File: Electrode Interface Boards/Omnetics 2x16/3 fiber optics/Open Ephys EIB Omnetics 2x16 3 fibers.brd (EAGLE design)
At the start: 16.1 x 16.1 mm, 40 parts

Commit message: Add Gerber files and images for EIBs
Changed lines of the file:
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@@
 <?xml version="1.0" encoding="utf-8"?>
 <!DOCTYPE eagle SYSTEM "eagle.dtd">
-<eagle version="6.1">
+<eagle version="6.3">
 <drawing>
 <settings>
@@
 <setting verticaltext="up"/>
 </settings>
-<grid distance="5" unitdist="mil" unit="mil" style="lines" multiple="1" display="yes" altdistance="0.005" altunitdist="inch" altunit="inch"/>
+<grid distance="1" unitdist="mil" unit="mil" style="lines" multiple="1" display="yes" altdistance="0.005" altunitdist="inch" altunit="inch"/>
 <layers>
-<layer number="1" name="Top" color="4" fill="1" visible="yes" active="yes"/>
+<layer number="1" name="Top" color="11" fill="1" visible="yes" active="yes"/>
 <layer number="16" name="Bottom" color="1" fill="1" visible="yes" active="yes"/>
 <layer number="17" name="Pads" color="2" fill="1" visible="yes" active="yes"/>
@@
 <layer number="23" name="tOrigins" color="15" fill="1" visible="yes" active="yes"/>
 <layer number="24" name="bOrigins" color="15" fill="1" visible="yes" active="yes"/>
-<layer number="25" name="tNames" color="7" fill="1" visible="yes" active="yes"/>
+<layer number="25" name="tNames" color="3" fill="1" visible="yes" active="yes"/>
 <layer number="26" name="bNames" color="7" fill="1" visible="yes" active="yes"/>
 <layer number="27" name="tValues" color="7" fill="1" visible="yes" active="yes"/>
@@
 <wire x1="19.685" y1="20.193" x2="21.082" y2="19.05" width="0.254" layer="25"/>
 <wire x1="21.082" y1="19.05" x2="21.844" y2="19.05" width="0.254" layer="25"/>
-<circle x="25.4" y="25.4" radius="8.0645" width="0.2032" layer="20"/>
+<circle x="25.4" y="25.4" radius="8.0645" width="0.0508" layer="20"/>
 <text x="20.701" y="26.416" size="1.143" layer="25" font="vector" ratio="15">fopt</text>
 <text x="21.082" y="23.368" size="1.143" layer="25" font="vector" ratio="15">eib</text>
@@
 </class>
 </classes>
-<designrules>
+<designrules name="default">
 <description language="de">&lt;b&gt;EAGLE Design Rules&lt;/b&gt;
 &lt;p&gt;

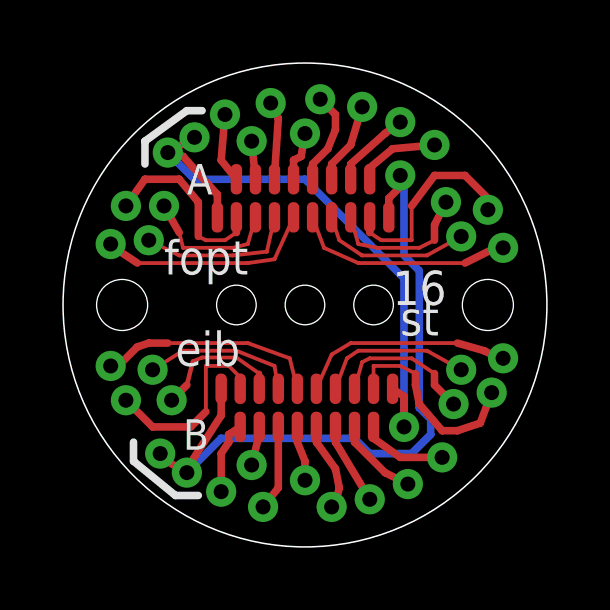
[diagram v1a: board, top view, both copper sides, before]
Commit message: Fix spacing issues on 2x16 boards
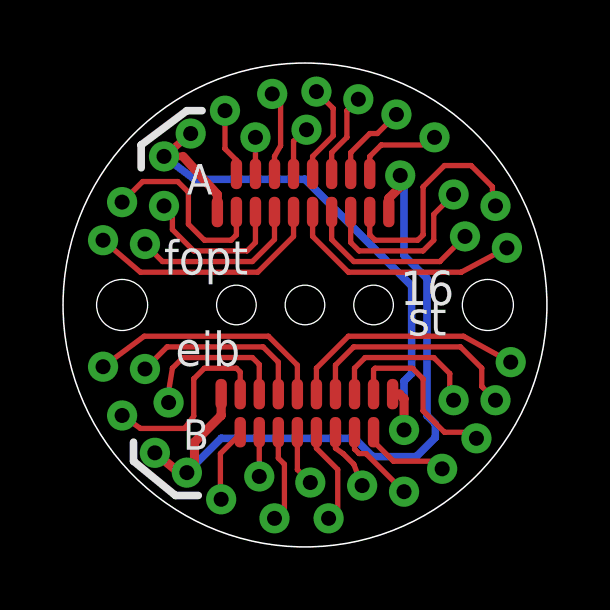
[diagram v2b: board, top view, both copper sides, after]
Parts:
- moved U$3 1.61 mm to (31.1, 21.0)
- moved U$4 1.53 mm to (31.8, 22.2)
- moved U$16 0.54 mm to (24.4, 18.3)
- moved U$10 0.52 mm to (19.3, 21.7)
- moved U$13 0.52 mm to (27.3, 19.4)
- moved U$17 0.46 mm to (23.9, 19.7)
- moved U$14 0.39 mm to (26.2, 18.3)
- moved U$11 0.38 mm to (30.0, 19.9)
- moved U$25 0.36 mm to (30.4, 29.1)
- moved U$34 0.31 mm to (24.3, 32.4)
- moved U$29 0.28 mm to (27.2, 32.3)
- moved U$6 0.28 mm to (32.3, 23.5)
- moved U$26 0.28 mm to (31.8, 28.7)
- moved U$12 0.28 mm to (28.7, 19.2)
- moved U$28 0.28 mm to (28.4, 31.8)
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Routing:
- net N$5: track 5.14 -> 7.65 mm
- net N$7: track 7.14 -> 8.18 mm
- net N$19: track 6.87 -> 7.87 mm
- net N$3: track 6.81 -> 5.86 mm
- net N$20: track 4.90 -> 5.85 mm
- net N$8: track 5.12 -> 6.03 mm
- net N$9: track 4.45 -> 5.31 mm
- net N$6: track 7.17 -> 8.00 mm
- net N$21: track 5.19 -> 6.01 mm
- net N$23: track 7.29 -> 8.05 mm
- net N$16: track 2.73 -> 2.11 mm
- net N$22: track 7.44 -> 7.99 mm
- net N$4: track 4.80 -> 5.35 mm
- net N$24: track 5.23 -> 5.78 mm
